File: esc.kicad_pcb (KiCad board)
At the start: 2 copper layers, 59 parts, among them IC1 4N25, IC2 LM25101, IC3 LM25101, IC4 LM25101, IC5 ATMEGA8-AI, P1 CONN_01X03, P2 CONN_01X03, P3 CONN_01X02, P4 CONN_02X02, Q1 MOSFET_N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

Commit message: PCB works...
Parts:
- added P4: CONN_02X02, Socket_Strips:Socket_Strip_Straight_2x02, F.Cu at (0.00, 0.00)
- added R17: 0 Bridge, Resistors_SMD:R_0805_HandSoldering, F.Cu at (0.00, 0.00)
- D1, R1, R6: moved to B.Cu
- Q1, Q10, Q11, Q12, Q2, Q3, Q4, Q5, Q6, Q7, Q8, Q9: footprint toni:SO8_WITH_EP -> sven:SO8_WITH_Heatpipes
- moved Q12 134.7 mm to (226.6, 69.1)
- moved Q9 132.6 mm to (226.6, 61.0)
- moved Q11 130.4 mm to (220.5, 69.1)
- moved Q10 124.6 mm to (220.5, 61.0)
- moved Q8 121.4 mm to (226.6, 77.5), turned to 180 degrees
- moved Q7 116.6 mm to (220.5, 77.5), turned to 180 degrees
- moved Q5 115.2 mm to (226.6, 85.9), turned to 180 degrees
- moved C3 108.6 mm to (217.9, 54.4), turned to 90 degrees
- moved Q6 108.4 mm to (220.5, 85.9), turned to 180 degrees
- moved P3 101.3 mm to (203.7, 52.8)
- moved C11 92.2 mm to (214.1, 60.5), turned to 180 degrees
- moved C4 83.8 mm to (201.7, 66.5), turned to 270 degrees
- moved C6 83.5 mm to (210.3, 65.3), turned to 270 degrees
- moved IC1 83.2 mm to (196.3, 100.8)
- moved C5 72.3 mm to (201.7, 71.1), turned to 90 degrees
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- renumbered R17 to Bridge, P4 to Switch
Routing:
- net V_BAT: track 0.00 -> 109.0 mm, vias 0 -> 2
- net GND: track 0.00 -> 80.8 mm, vias 0 -> 1
- net 9V: track 0.00 -> 80.2 mm, vias 0 -> 7
- net /C_Highside_Gate: track 0.00 -> 21.5 mm, vias 0 -> 3
- net C: track 0.00 -> 21.2 mm, vias 0 -> 2
- net /C_Lowside_Gate: track 0.00 -> 19.5 mm, vias 0 -> 3
- net /B_Lowside_Gate: track 0.00 -> 17.4 mm, vias 0 -> 3
- net /B_Highside_Gate: track 0.00 -> 16.0 mm, vias 0 -> 3
- net /VBat_to_10V: track 0.00 -> 15.7 mm
- net A: track 13.7 -> 28.2 mm
- net B: track 0.00 -> 10.6 mm
- net Net-(C4-Pad1): track 0.00 -> 6.62 mm, vias 0 -> 1
- net /INPUT_GND: track 0.00 -> 5.37 mm
- net +5V: track 0.00 -> 3.84 mm
- net Net-(C8-Pad1): track 0.00 -> 3.82 mm
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- added copper zone on F.Cu, net A
- added copper zone on F.Cu, net B
- added copper zone on F.Cu, net C
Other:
- net class VBat added: clearance 0.381, trace_width 0.254, via_dia 0.889, via_drill 0.635
- rule via_min_size: 0.889 -> 0.762
- board text added: ">_"
- board text added: "Brushless ESC 30A"

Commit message: PCB weiter+Layout R
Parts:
- removed Bridge: 0 Bridge, Resistors_SMD:R_0805_HandSoldering
- removed Switch: CONN_02X02, Socket_Strips:Socket_Strip_Straight_2x02
- added R10: R, Resistors_SMD:R_0603_HandSoldering, F.Cu at (215.1, 92.7)
- added R18: R, Resistors_SMD:R_0603_HandSoldering, B.Cu at (215.9, 102.9)
- added R19: R, Resistors_SMD:R_0603_HandSoldering, B.Cu at (214.9, 83.3)
- added R20: R, Resistors_SMD:R_0603_HandSoldering, B.Cu at (214.6, 76.5)
- added R21: R, Resistors_SMD:R_0603_HandSoldering, B.Cu at (215.6, 62.0)
- added R22: R, Resistors_SMD:R_0603_HandSoldering, B.Cu at (215.6, 70.6)
- C14, C15, C16: footprint Capacitors_SMD:C_0805_HandSoldering -> Capacitors_SMD:C_0603_HandSoldering
- R11, R13, R14, R15, R3, R4, R5, R8, R9: footprint Resistors_SMD:R_0805_HandSoldering -> Resistors_SMD:R_0603_HandSoldering
- R12: footprint Resistors_SMD:R_0805_HandSoldering -> Resistors_SMD:R_0603_HandSoldering; moved to B.Cu
- R17: moved to B.Cu
- moved R17 212.8 mm to (194.3, 86.9), turned to 180 degrees
- moved P4 204.2 mm to (196.8, 54.4), turned to 180 degrees
- moved R12 43.6 mm to (198.6, 84.1), turned to 180 degrees
- moved C15 39.6 mm to (199.6, 91.7), turned to 270 degrees
- moved R3 38.8 mm to (194.8, 89.7), turned to 180 degrees
- moved C16 35.4 mm to (197.9, 90.7), turned to 270 degrees
- moved C14 30.6 mm to (201.4, 93.0), turned to 90 degrees
- moved R13 27.2 mm to (194.8, 93.7), turned to 180 degrees
- moved R8 24.9 mm to (194.8, 91.7), turned to 180 degrees
- moved C7 21.8 mm to (191.0, 71.9)
- moved C13 21.3 mm to (201.4, 83.3), turned to 270 degrees
- moved R15 14.9 mm to (204.7, 127.5)
- moved C10 13.5 mm to (188.0, 79.2)
- moved C12 8.13 mm to (175.3, 91.4)
- moved R9 5.55 mm to (200.4, 123.4)
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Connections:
- IC2 pad 3: /A_Highside_Gate -> Net-(IC2-Pad3)
- IC2 pad 8: /A_Lowside_Gate -> Net-(IC2-Pad8)
- IC3 pad 3: /B_Highside_Gate -> Net-(IC3-Pad3)
- IC3 pad 8: /B_Lowside_Gate -> Net-(IC3-Pad8)
- IC4 pad 3: /C_Highside_Gate -> Net-(IC4-Pad3)
- IC4 pad 8: /C_Lowside_Gate -> Net-(IC4-Pad8)
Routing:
- net A+: track 0.00 -> 41.2 mm
- net C-: track 0.00 -> 40.1 mm, vias 0 -> 4
- net GND: track 80.8 -> 118.8 mm, vias 1 -> 7
- net +5V: track 3.84 -> 39.2 mm, vias 0 -> 3
- net A-: track 0.00 -> 31.7 mm
- net S_B: track 0.00 -> 31.0 mm, vias 0 -> 2
- net C+: track 0.00 -> 30.9 mm, vias 0 -> 2
- net S_C: track 0.00 -> 25.8 mm, vias 0 -> 2
- net B+: track 0.00 -> 25.4 mm
- net B-: track 0.00 -> 23.5 mm
- net S_A: track 0.00 -> 20.0 mm, vias 0 -> 2
- net S_PWR: track 0.00 -> 18.4 mm, vias 0 -> 2
- net V_BAT: track 109.0 -> 125.1 mm
- net /C_Highside_Gate: track 21.5 -> 9.99 mm, vias 3 -> 2
- net M: track 0.00 -> 9.48 mm
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- added copper zone on B.Cu, net A
- added copper zone on B.Cu, net B
- added copper zone on B.Cu, net C

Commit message: PCB almost done!
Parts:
- R16, R7: footprint Resistors_SMD:R_0805_HandSoldering -> Resistors_SMD:R_0603_HandSoldering
- moved R14 70.6 mm to (231.9, 75.2), turned to 0 degrees
- moved R9 48.8 mm to (232.7, 86.9)
- moved R4 42.8 mm to (214.9, 103.6), turned to 180 degrees
- moved R5 32.6 mm to (204.0, 95.8)
- moved C12 29.6 mm to (203.7, 83.3)
- moved R15 27.2 mm to (204.0, 100.3), turned to 0 degrees
- moved R11 23.3 mm to (204.0, 97.8), turned to 0 degrees
- moved R7 12.5 mm to (187.5, 73.2)
- moved R16 8.70 mm to (191.0, 74.4)
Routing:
- net S_C: track 25.8 -> 107.0 mm, vias 2 -> 4
- net S_B: track 31.0 -> 102.2 mm, vias 2 -> 4
- net B: track 10.6 -> 52.3 mm, vias 0 -> 8
- net A: track 28.2 -> 69.5 mm, vias 2 -> 10
- net C: track 21.2 -> 55.9 mm, vias 2 -> 10
- net S_A: track 20.0 -> 52.1 mm, vias 2 -> 4
- net PWM: track 3.12 -> 32.3 mm, vias 0 -> 1
- net GND: track 118.8 -> 144.9 mm, vias 7 -> 8
- net +5V: track 39.2 -> 62.2 mm, vias 3 -> 5
- net Net-(C12-Pad1): track 0.00 -> 5.74 mm
- net Net-(IC5-Pad29): track 0.00 -> 5.53 mm
- net S_PWR: track 18.4 -> 20.8 mm

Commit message: PCB V1.0
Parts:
- added P5: CONN_01X01, Connect:1pin, F.Cu at (204.7, 73.4)
- added P6: CONN_01X01, Connect:1pin, F.Cu at (189.2, 53.1)
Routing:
- net GND: track 144.9 -> 261.4 mm, vias 8 -> 13
- net V_BAT: track 125.1 -> 163.0 mm, vias 2 -> 3
- net /C_Highside_Gate: track 9.99 -> 16.8 mm
- net Net-(IC4-Pad3): track 0.00 -> 2.57 mm, vias 0 -> 1
- net S_B: track 102.2 -> 103.0 mm
- added copper zone on B.Cu, net GND
- added copper zone on F.Cu, net GND
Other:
- board outline added: 50 x 60.5 mm

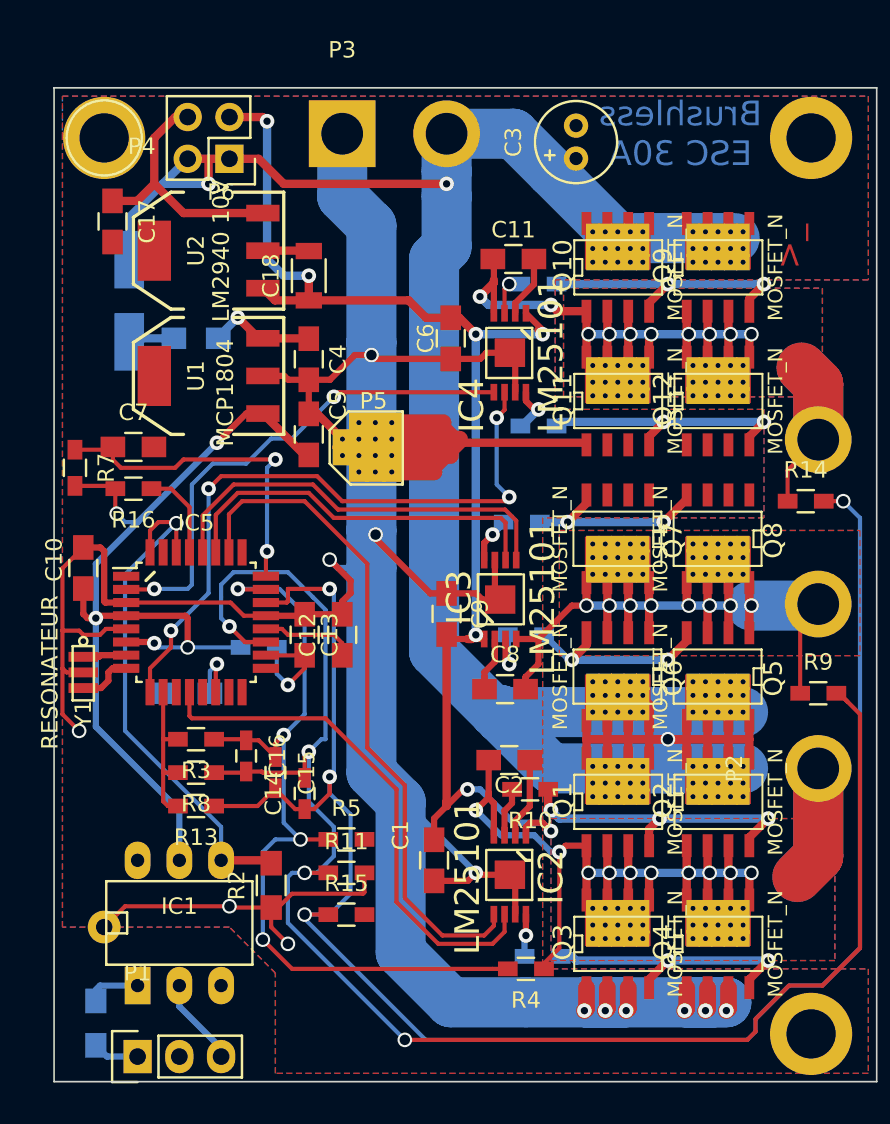
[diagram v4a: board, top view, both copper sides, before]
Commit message: Added pull down Resistors
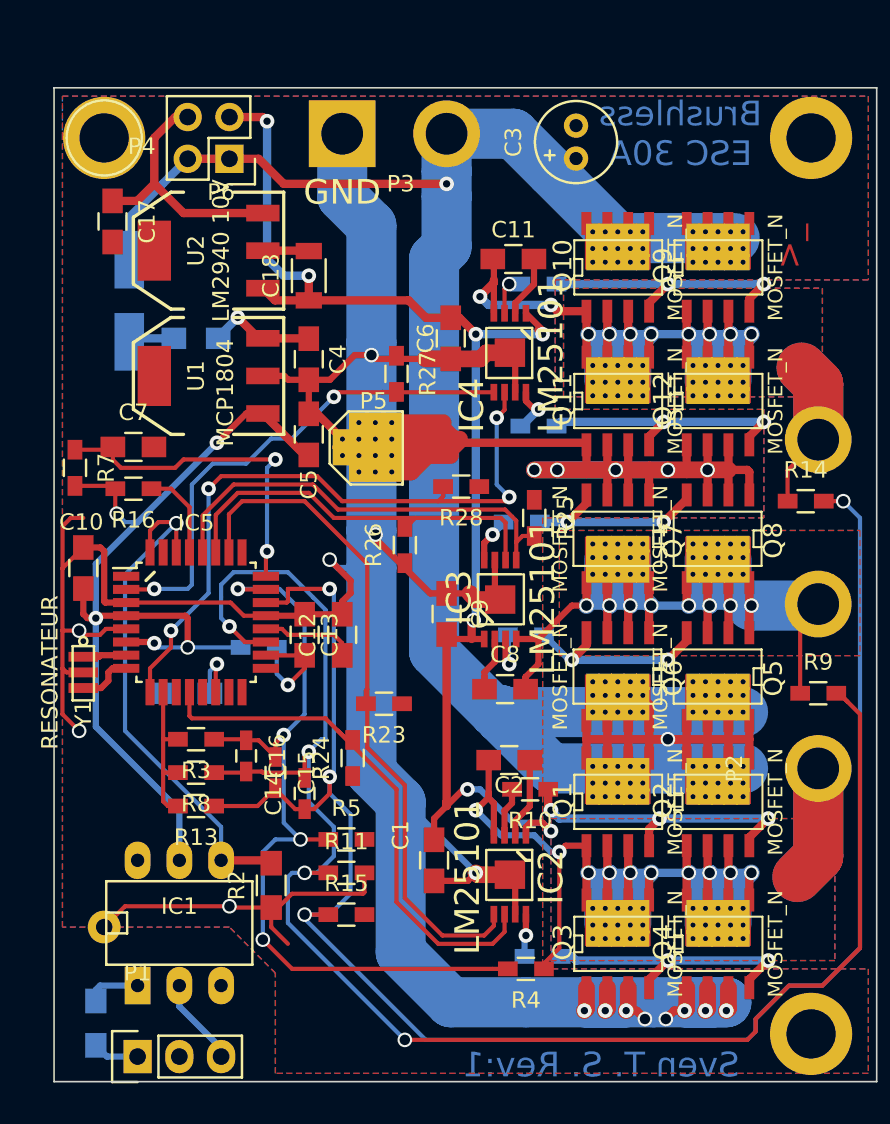
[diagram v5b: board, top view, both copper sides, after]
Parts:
- added R23: PD, Resistors_SMD:R_0603_HandSoldering, F.Cu at (206.2, 87.5)
- added R24: PD, Resistors_SMD:R_0603_HandSoldering, F.Cu at (204.3, 90.8)
- added R25: PD, Resistors_SMD:R_0603_HandSoldering, F.Cu at (215.4, 76.2)
- added R26: PD, Resistors_SMD:R_0603_HandSoldering, F.Cu at (207.5, 77.9)
- added R27: PD, Resistors_SMD:R_0603_HandSoldering, F.Cu at (207.0, 67.4)
- added R28: PD, Resistors_SMD:R_0603_HandSoldering, F.Cu at (210.9, 74.3)
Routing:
- net GND: track 261.4 -> 322.8 mm, vias 13 -> 20
- net A: track 69.5 -> 102.5 mm
- net C: track 55.9 -> 86.5 mm
- net B: track 52.3 -> 82.9 mm
- net V_BAT: track 163.0 -> 158.7 mm, vias 3 -> 2
- net B+: track 25.4 -> 26.7 mm
- net A-: track 31.7 -> 32.9 mm
- net C-: track 40.1 -> 41.1 mm
- net A+: track 41.2 -> 42.1 mm
- net C+: track 30.9 -> 31.8 mm
- net B-: track 23.5 -> 24.3 mm
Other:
- board text added: "(C) Sven T. Schneider"
- board text added: "GND"
- board text added: "Sven T. S. Rev:1"

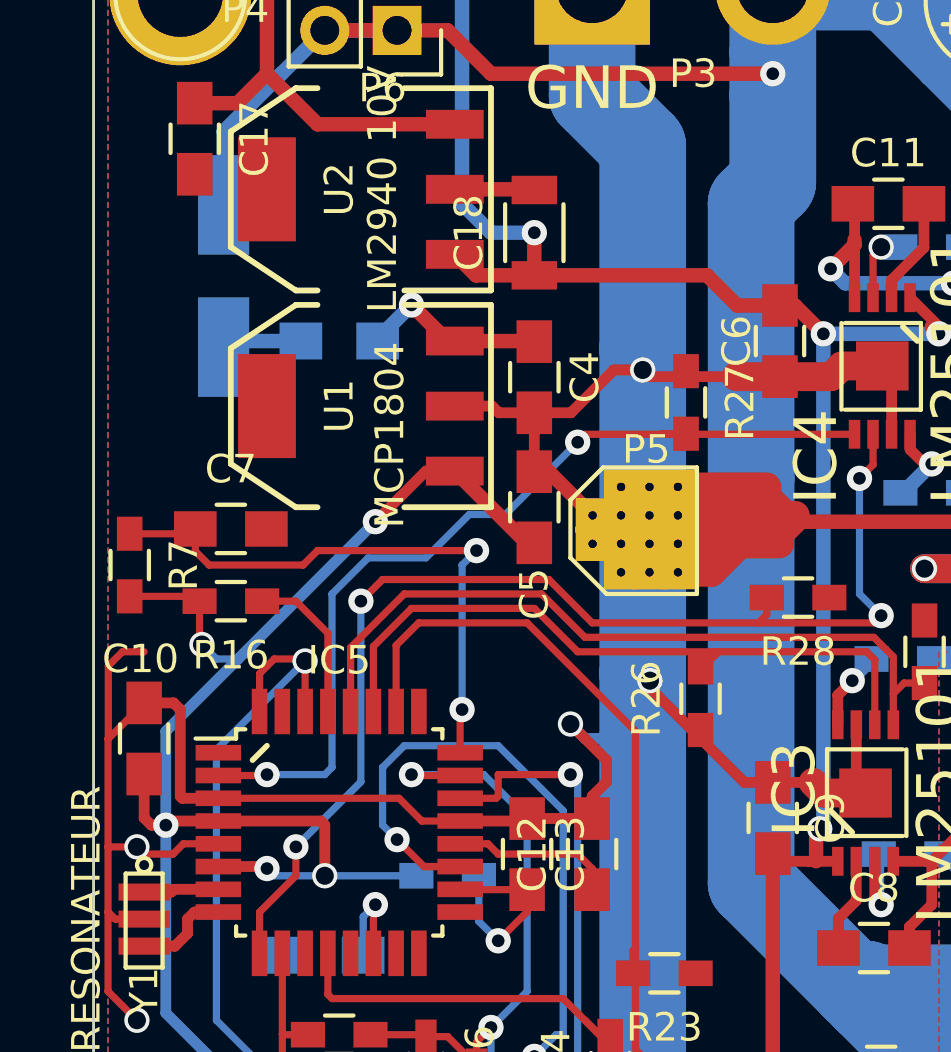
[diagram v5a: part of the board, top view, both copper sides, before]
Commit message: Reduced part count, Splittet 22uF cap C17 into two 10uF
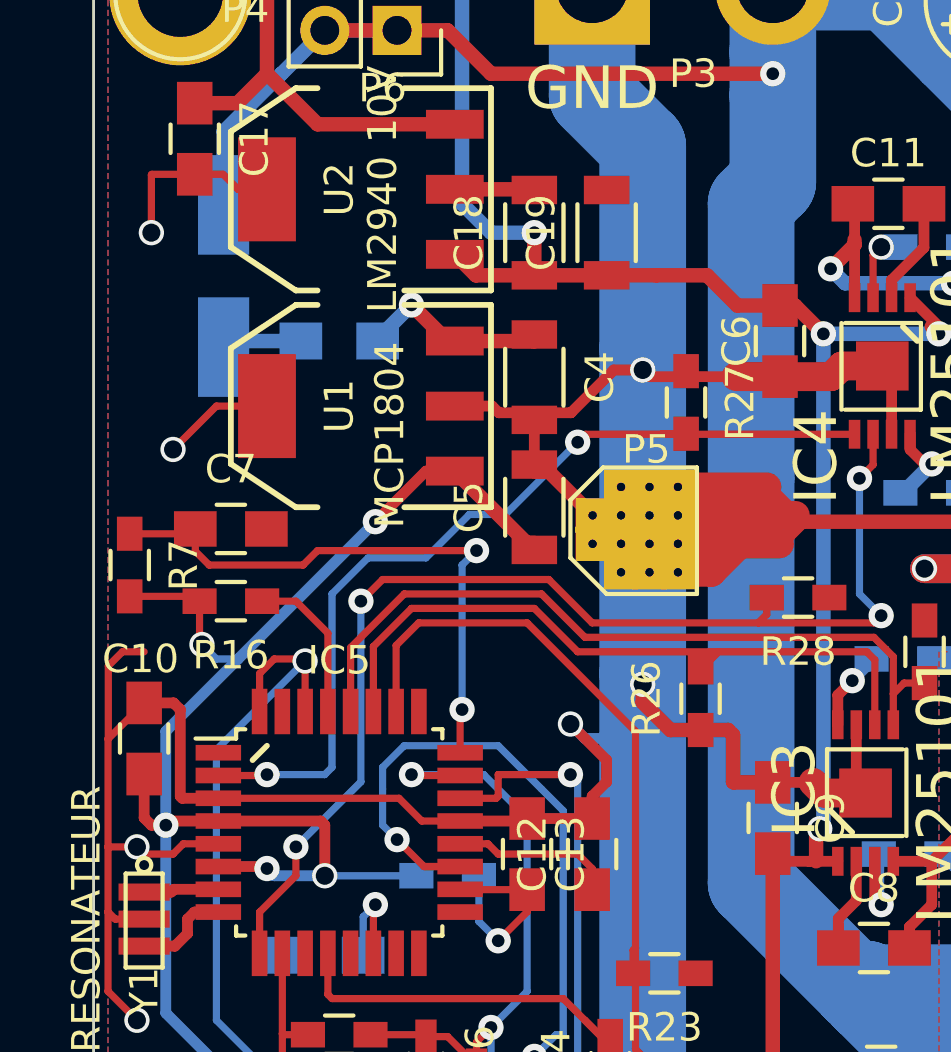
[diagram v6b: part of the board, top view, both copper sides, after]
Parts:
- added C19: 10µ, Capacitors_SMD:C_1206, F.Cu at (204.2, 61.5)
- C18: value 22µ -> 10µ
- C4, C5: footprint Capacitors_SMD:C_0805_HandSoldering -> Capacitors_SMD:C_1206
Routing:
- net GND: track 322.8 -> 334.4 mm, vias 20 -> 22
- net 9V: track 80.0 -> 81.7 mm

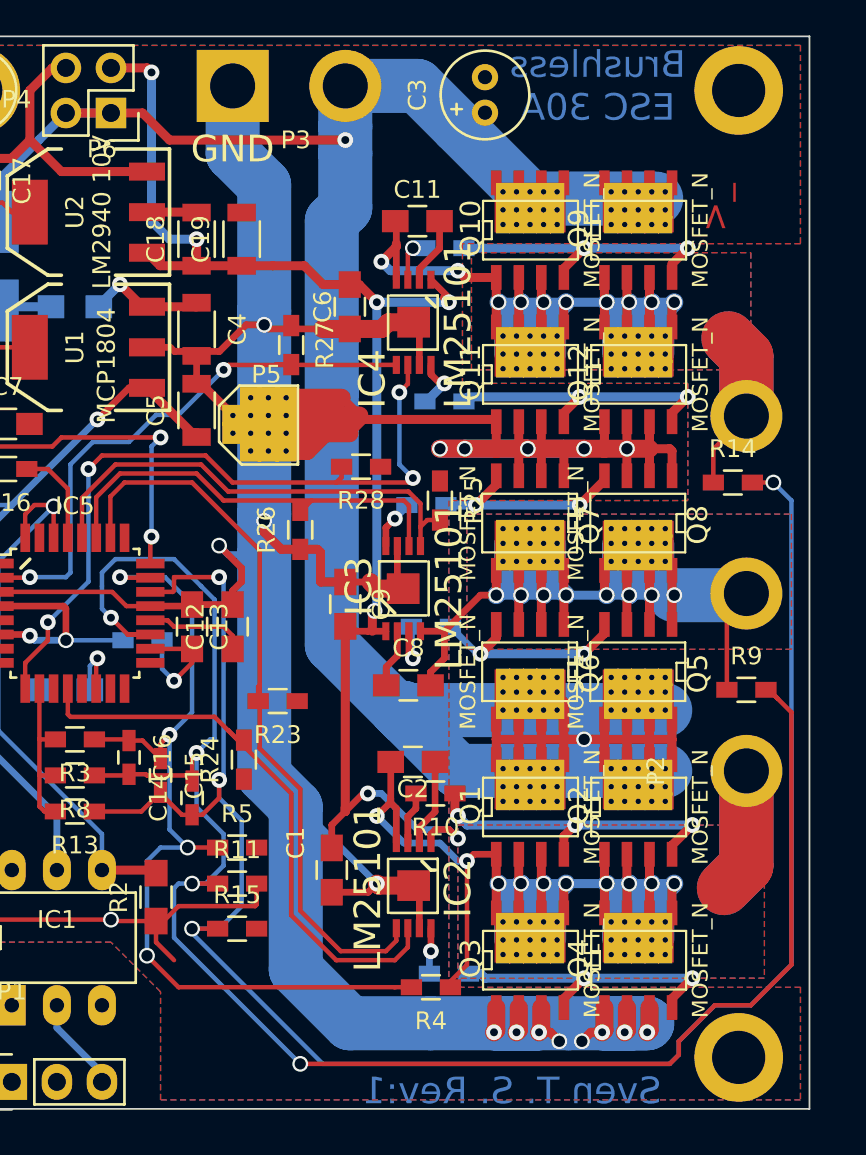
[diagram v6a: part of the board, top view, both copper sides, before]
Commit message: Added suport for Anderson PowerPole as input connectors.
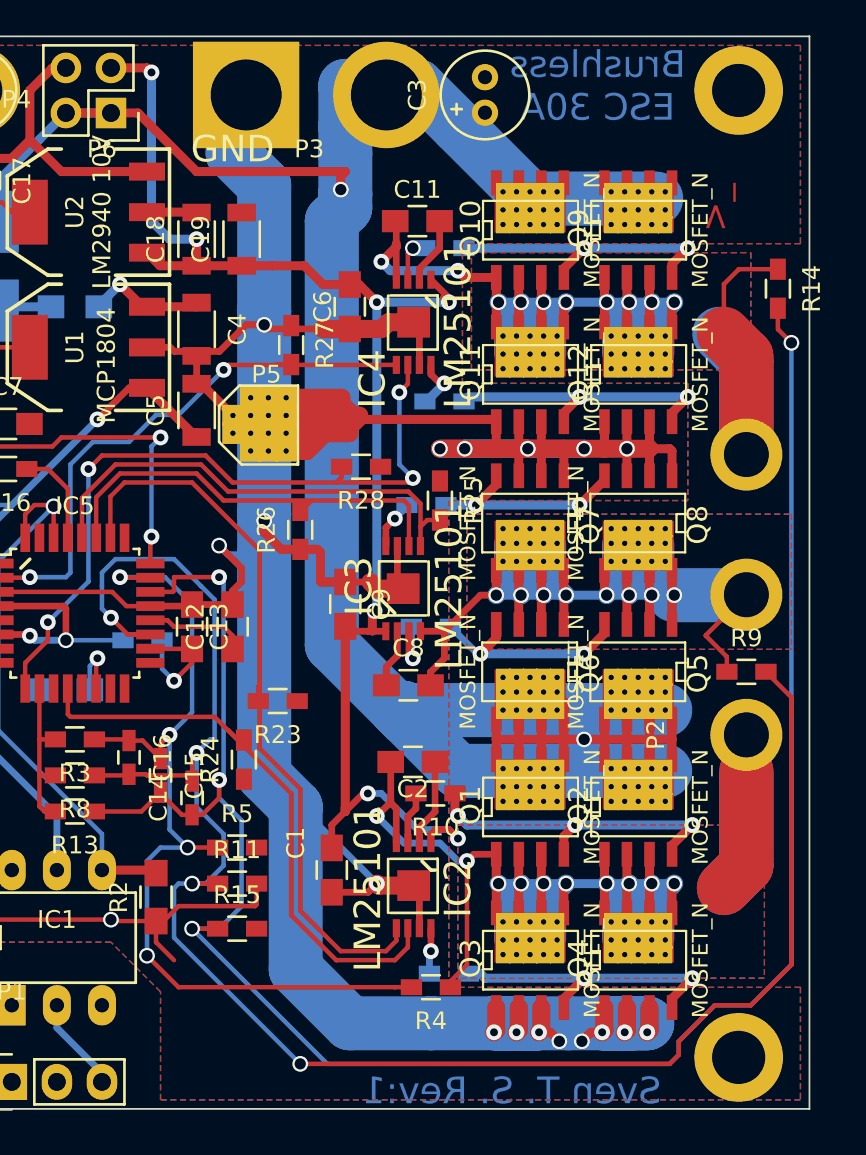
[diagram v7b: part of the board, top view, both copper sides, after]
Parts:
- moved R14 11.2 mm to (234.4, 64.3), turned to 270 degrees
- moved P2 2.03 mm to (232.7, 89.4)
- moved R9 1.02 mm to (232.7, 85.9)
- moved P3 0.92 mm to (204.5, 53.3)
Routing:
- net S_C: track 107.0 -> 115.2 mm
- net C: track 86.5 -> 93.4 mm
- net V_BAT: track 158.7 -> 161.9 mm
- net B: track 82.9 -> 84.3 mm
